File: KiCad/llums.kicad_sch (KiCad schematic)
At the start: 19 parts, among them J1 CONNECTOR_MOTOR, K1 Relay_SPST-NO, Q2 IRLZ44N, Q3 IRLZ44N, Q4 IRLZ44N, Q5 IRLZ44N, Q6 IRLZ44N, Q7 IRLZ44N

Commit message: alguns errors de CADLAB i he canivat d'ordre els LEDs i els drivers a la PCB.
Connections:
- net RELÉ: now reaches D7.1 (K), K1.A2, Q7.2 (D)
- net C_LED6: now reaches D6.1 (K), Q6.2 (D)
- net C_LED2: now reaches D2.1 (K), Q3.2 (D)
- net A_LED2: now reaches D2.2 (A), R2.1
- net MOTOR: now reaches J1.1 (Pin_1), K1.14
- net A_LED5: now reaches D5.2 (A), R5.1
- net A_LED4: now reaches D4.2 (A), R4.1
- net C_LED4: now reaches D4.1 (K), Q5.2 (D)
- net A_LED3: now reaches D3.2 (A), R3.1
- net C_LED3: now reaches D3.1 (K), Q2.2 (D)
- net C_LED5: now reaches D5.1 (K), Q4.2 (D)
- net A_LED6: now reaches D6.2 (A), R6.1

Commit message: Relé??
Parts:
- K1: footprint (none) -> Relay_SMD:Relay_DPDT_Omron_G6S-2F
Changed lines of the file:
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@@
 			)
 		)
-		(property "Footprint" ""
+		(property "Footprint" "Relay_SMD:Relay_DPDT_Omron_G6S-2F"
 			(at 179.07 139.7 0)
 			(effects

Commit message: presentar
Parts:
- removed K1: Relay_SPST-NO, Relay_SMD:Relay_DPDT_Omron_G6S-2F, symbol Relay:Relay_SPST-NO
- added K1: Fujitsu_FTR-LYAA005x, Relay_SMD:Relay_DPDT_Omron_G6S-2F, symbol Relay:Fujitsu_FTR-LYAA005x
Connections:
- net +12V: now also K1.13, K1.A1
- net MOTOR: now also K1.14
- net RELÉ: now also K1.A2
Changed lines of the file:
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@@
+	)
+	(symbol
+		(lib_id "Relay:Fujitsu_FTR-LYAA005x")
+		(at 180.34 128.27 270)
+		(unit 1)
+		(exclude_from_sim no)
+		(in_bom yes)
+		(on_board yes)
+		(dnp no)
+		(fields_autoplaced yes)
+		(property "Reference" "K1"
+			(at 180.34 113.03 90)
+			(effects
+				(font
+					(size 1.27 1.27)
+				)
+			)
+		)
+		(property "Value" "Fujitsu_FTR-LYAA005x"
+			(at 180.34 115.57 90)
+			(effects
+				(font
+					(size 1.27 1.27)
+				)
+			)
+		)
+		(property "Footprint" "Relay_SMD:Relay_DPDT_Omron_G6S-2F"
+			(at 179.07 139.7 0)
+			(effects
+				(font
+					(size 1.27 1.27)
+				)
+				(justify left)
+				(hide yes)
+			)
+		)
+		(property "Datasheet" "https://www.fujitsu.com/sg/imagesgig5/ftr-ly.pdf"
+			(at 176.53 146.05 0)
+			(effects
+				(font
+					(size 1.27 1.27)
+				)
+				(justify left)
+				(hide yes)
+			)
+		)
+		(property "Description" "Relay, SPST Form A, vertical mount, 5-60V coil, 6A, 250VAC, 28 x 5 x 15mm"
+			(at 180.34 128.27 0)
+			(effects
+				(font
+					(size 1.27 1.27)
+				)
+				(hide yes)
+			)
+		)
+		(pin "13"
+		)
+		(pin "14"
+		)
+		(pin "A2"
+		)
+		(pin "A1"
+		)
+		(instances
+			(project ""
+				(path "/b4874c87-978f-427f-bc45-3635f8629977/0edcf3aa-0722-4786-beaa-59b728b7a9fc"
+					(reference "K1")
+					(unit 1)
+				)
+			)
+		)
 	)
 	(symbol
@@
 					(unit 1)
 				)
-			)
-		)
-	)
-	(symbol
-		(lib_id "Relay:Relay_SPST-NO")
-		(at 180.34 128.27 270)
-		(unit 1)
-		(exclude_from_sim no)
-		(in_bom yes)
-		(on_board yes)
-		(dnp no)
-		(fields_autoplaced yes)
-		(property "Reference" "K1"
-			(at 180.34 113.03 90)
-			(effects
-				(font
-					(size 1.27 1.27)
-				)
-			)
-		)
-		(property "Value" "Relay_SPST-NO"
-			(at 180.34 115.57 90)
-			(effects
-				(font
-					(size 1.27 1.27)
-				)
-			)
-		)
-		(property "Footprint" "Relay_SMD:Relay_DPDT_Omron_G6S-2F"
-			(at 179.07 139.7 0)
-			(effects
-				(font
-					(size 1.27 1.27)
-				)
-				(justify left)
-				(hide yes)
-			)
-		)
-		(property "Datasheet" "~"
-			(at 180.34 128.27 0)
-			(effects
-				(font
-					(size 1.27 1.27)
-				)
-				(hide yes)
-			)
-		)
-		(property "Description" "Relay SPST, normally open, EN50005"
-			(at 180.34 128.27 0)
-			(effects
-				(font
-					(size 1.27 1.27)
-				)
-				(hide yes)
-			)
-		)
-		(pin "13"
-		)
-		(pin "14"
-		)
-		(pin "A1"
-		)
-		(pin "A2"
-		)
-		(instances
-			(project ""
-				(path "/b4874c87-978f-427f-bc45-3635f8629977/0edcf3aa-0722-4786-beaa-59b728b7a9fc"
-					(reference "K1")
-					(unit 1)
-				)

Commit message: correccions Manel
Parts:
- K1: footprint Relay_SMD:Relay_DPDT_Omron_G6S-2F -> Relay_THT:Relay_1-Form-C_Schrack-RYII_RM3.2mm
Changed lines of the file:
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@@
 			)
 		)
-		(property "Footprint" "Relay_SMD:Relay_DPDT_Omron_G6S-2F"
+		(property "Footprint" "Relay_THT:Relay_1-Form-C_Schrack-RYII_RM3.2mm"
 			(at 179.07 139.7 0)
 			(effects

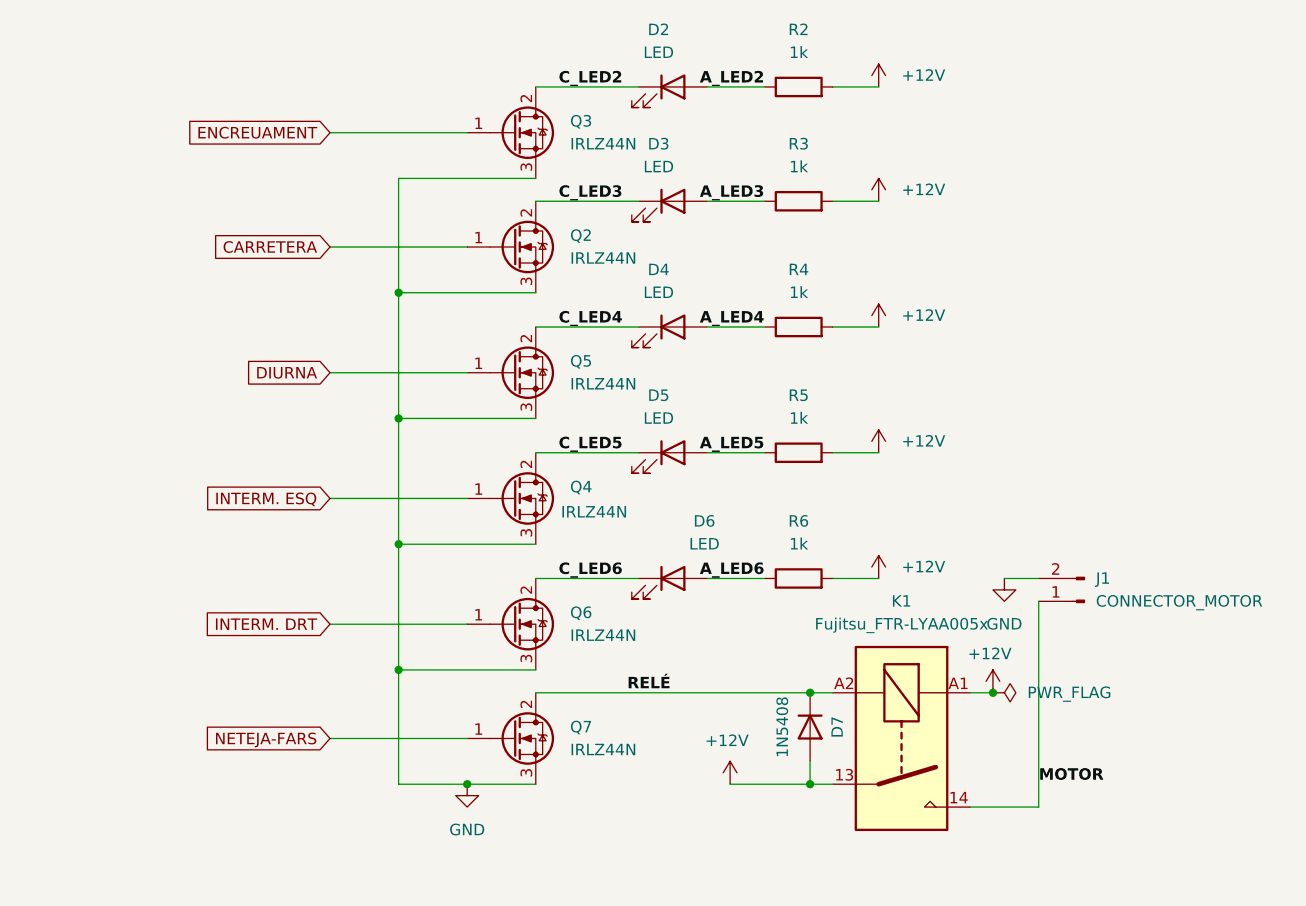
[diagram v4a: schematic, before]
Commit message: Connectors amb huellas
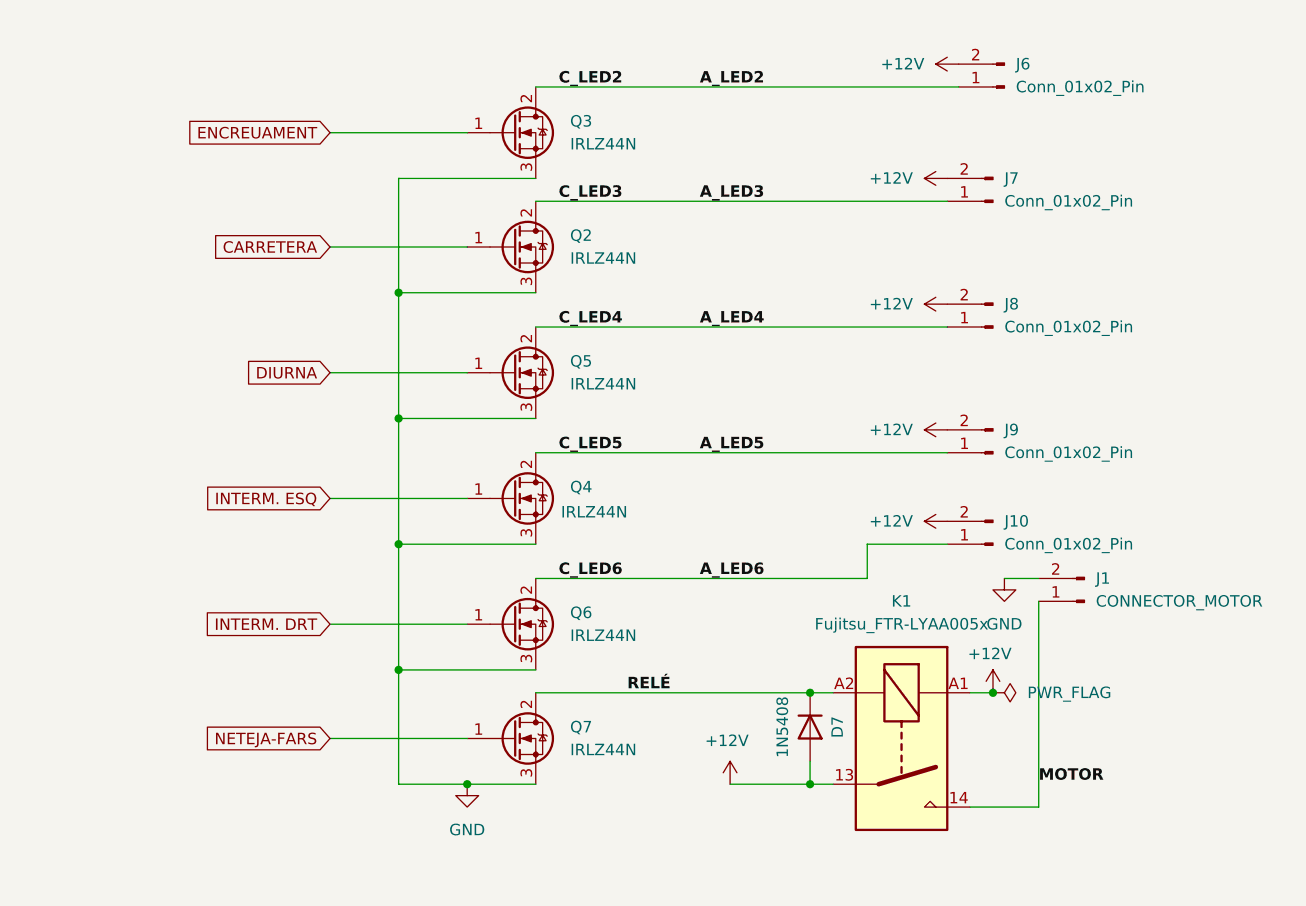
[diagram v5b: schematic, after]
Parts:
- removed D2, D3, D4, D5, D6: LED, LED_THT:LED_D5.0mm, symbol Device:LED
- removed R2, R3, R4, R5, R6: 1k, Relay_SMD:Relay_2P2T_10x6mm_TE_IMxxG, symbol Device:R
- added J10, J7, J8, J9: Conn_01x02_Pin, TerminalBlock:TerminalBlock_MaiXu_MX126-5.0-02P_1x02_P5.00mm, symbol Connector:Conn_01x02_Pin
- added J6: Conn_01x02_Pin, TerminalBlock_Phoenix:TerminalBlock_Phoenix_MKDS-1,5-2-5.08_1x02_P5.08mm_Horizontal, symbol Connector:Conn_01x02_Pin
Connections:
- net C_LED2 is gone; now on net A_LED2: Q3.2 (D)
- net C_LED3 is gone; now on net A_LED3: Q2.2 (D)
- net C_LED4 is gone; now on net A_LED4: Q5.2 (D)
- net C_LED5 is gone; now on net A_LED5: Q4.2 (D)
- net C_LED6 is gone; now on net A_LED6: Q6.2 (D)
- net +12V: now also J10.2 (Pin_2), J6.2 (Pin_2), J7.2 (Pin_2), J8.2 (Pin_2), J9.2 (Pin_2)
- net A_LED2: now also J6.1 (Pin_1)
- net A_LED3: now also J7.1 (Pin_1)
- net A_LED4: now also J8.1 (Pin_1)
- net A_LED5: now also J9.1 (Pin_1)
- net A_LED6: now also J10.1 (Pin_1)

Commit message: LLums finals amb resistències afegides
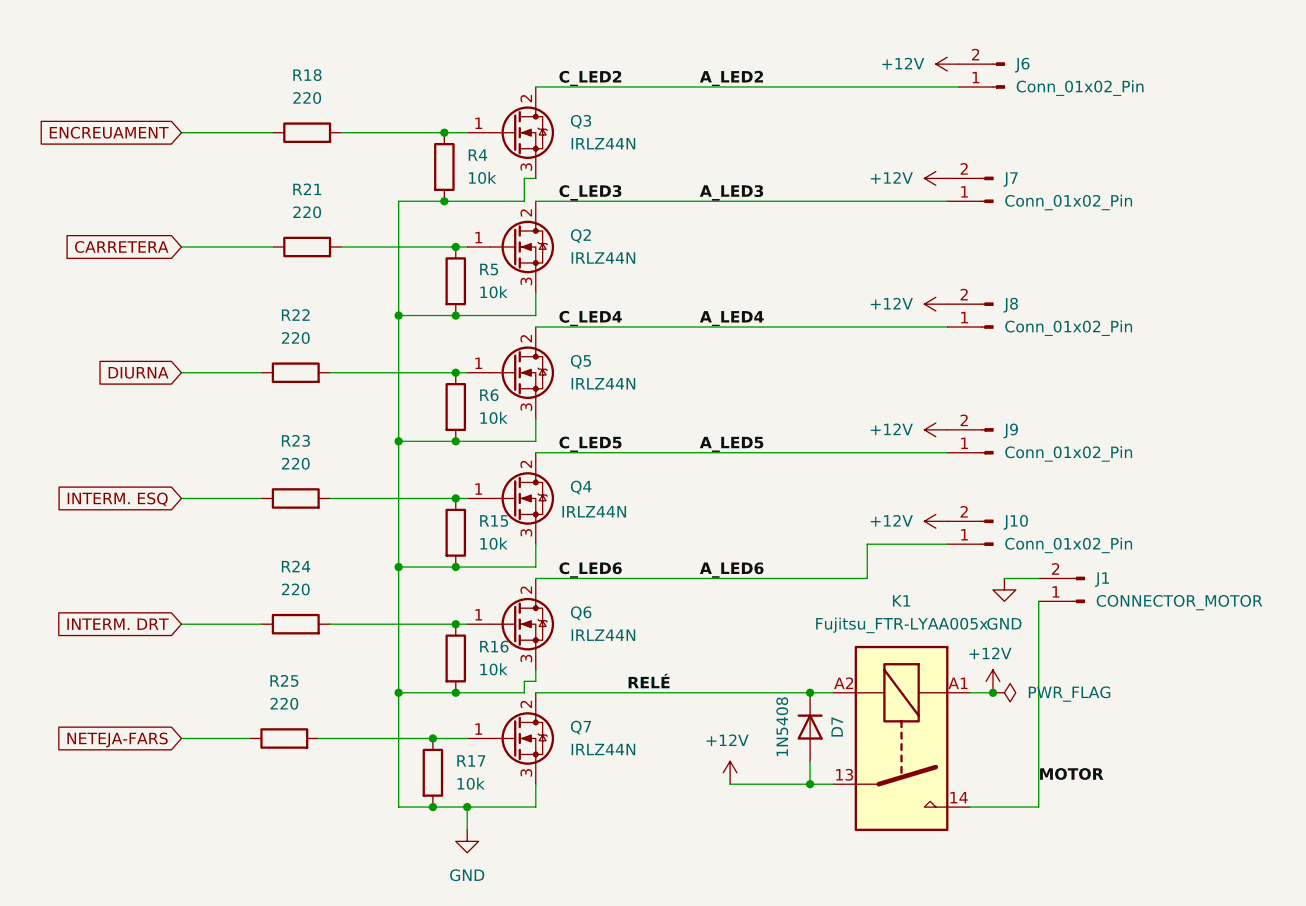
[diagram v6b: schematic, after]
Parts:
- added R15, R16, R17, R4, R5, R6: 10k, Resistor_SMD:R_0805_2012Metric_Pad1.20x1.40mm_HandSolder, symbol Device:R
- added R18, R21, R22, R23, R24, R25: 220, Resistor_SMD:R_0805_2012Metric_Pad1.20x1.40mm_HandSolder, symbol Device:R
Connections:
- net CARRETERA: now also R21.1; no longer Q2.1 (G)
- net DIURNA: now also R22.1; no longer Q5.1 (G)
- net ENCREUAMENT: now also R18.1; no longer Q3.1 (G)
- net GND: now also R15.2, R16.2, R17.2, R4.2, R5.2, R6.2
- net INTERM. DRT: now also R24.1; no longer Q6.1 (G)
- net INTERM. ESQ: now also R23.1; no longer Q4.1 (G)
- net NETEJA-FARS: now also R25.1; no longer Q7.1 (G)
- new net: Q3.1 (G), R18.2, R4.1
- new net: Q6.1 (G), R16.1, R24.2
- new net: Q2.1 (G), R21.2, R5.1
- new net: Q5.1 (G), R22.2, R6.1
- new net: Q7.1 (G), R17.1, R25.2
- new net: Q4.1 (G), R15.1, R23.2
